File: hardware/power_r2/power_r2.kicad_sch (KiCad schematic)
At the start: 52 parts, among them J101 FPC Connector, J102 Power Input, Q101 AONR21357, U101 SIC473

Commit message: Next revision of the boards are finished and ready for fabrication, and a BOM has been added.
The BOM is still missing components for the nucleo shield.
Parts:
- added TP106: GND Test Point, TestPoint:TestPoint_Pad_D1.5mm, symbol Connector:TestPoint
- C104, C105: Item Link https://www.digikey.com.au/en/products/detail/murata-electr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 -> https://www.digikey.com.au/en/products/detail/stmicroelectr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
- C106: value 100n -> 100n 100V; Item Link Use existing -> https://www.digikey.com.au/en/products/detail/stmicroelectr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
- C107, C108, C109, C110, C111, C112: Item Link Use existing -> https://www.digikey.com.au/en/products/detail/samsung-elect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
- C113, C115: Item Link (none) -> https://www.digikey.com.au/en/products/detail/murata-electr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
- C114: Item Link Use existing -> https://www.digikey.com.au/en/products/detail/murata-electr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
- C116: Item Link https://www.digikey.com.au/en/products/detail/tdk-corporati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 -> https://www.digikey.com.au/en/products/detail/murata-electr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
- C117: Item Link https://www.digikey.com.au/en/products/detail/w%C3%BCrth-el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 -> https://www.digikey.com.au/en/products/detail/yageo/CC0603J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
- C118: value 100n 50V -> 100n 100V; Item Link (none) -> https://www.digikey.com.au/en/products/detail/stmicroelectr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
- C119: value 100n -> 100n 100V; Item Link (none) -> https://www.digikey.com.au/en/products/detail/stmicroelectr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
- H101, H102, JP104, TP101, TP102, TP103, TP104, TP105: now left out of the parts list
- J101: Item Link (none) -> https://www.digikey.com.au/en/products/detail/cvilux-usa/CF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
- J102: Item Link (none) -> https://au.element14.com/jst-japan-solderless-terminals/s2b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
- JP101, JP102, JP103: footprint Jumper:SolderJumper-3_P1.3mm_Open_Pad1.0x1.5mm -> rave_shades:SolderJumper-3_P1.3mm_Open_Pad1.0x1.5mm; now left out of the parts list
- R101, R109, R114: value 10k -> 10k 1%; Item Link (none) -> https://www.digikey.com.au/en/products/detail/bourns-inc/CR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
- R102, R103, R104, R105, R106, R108, R111, R112: Item Link (none) -> https://www.digikey.com.au/en/products/detail/yageo/RC0402F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
- R107: Item Link (none) -> https://www.digikey.com.au/en/products/detail/bourns-inc/CR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
- R110: Item Link (none) -> https://www.digikey.com.au/en/products/detail/stackpole-ele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
- R113: Item Link (none) -> https://www.digikey.com.au/en/products/detail/koa-speer-ele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
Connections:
- net +5V: now also J101.7 (Pin_7); no longer J101.2 (Pin_2)
- net GND: now also TP106.1
- net SPARE_0_5V0: now also J101.2 (Pin_2); no longer J101.7 (Pin_7)
- net SPARE_1_5V0: now also J101.1 (Pin_1); no longer J101.8 (Pin_8)
- net +5V_OR_GND renamed 5V0_OR_GND
- net 5V0_OR_GND: now also J101.8 (Pin_8); no longer J101.1 (Pin_1)
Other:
- note added: "Over Current Protection Imax = 3 A R = 0.024 R Vmax = 32 V"
- note removed: "ESD Protection Imax = 3 A R = 0.024 R Vmax = 32 V"
- moved on the sheet: C101, C102, C103, C104, C105, C106, C107, C108, C109, C110, C111, C112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

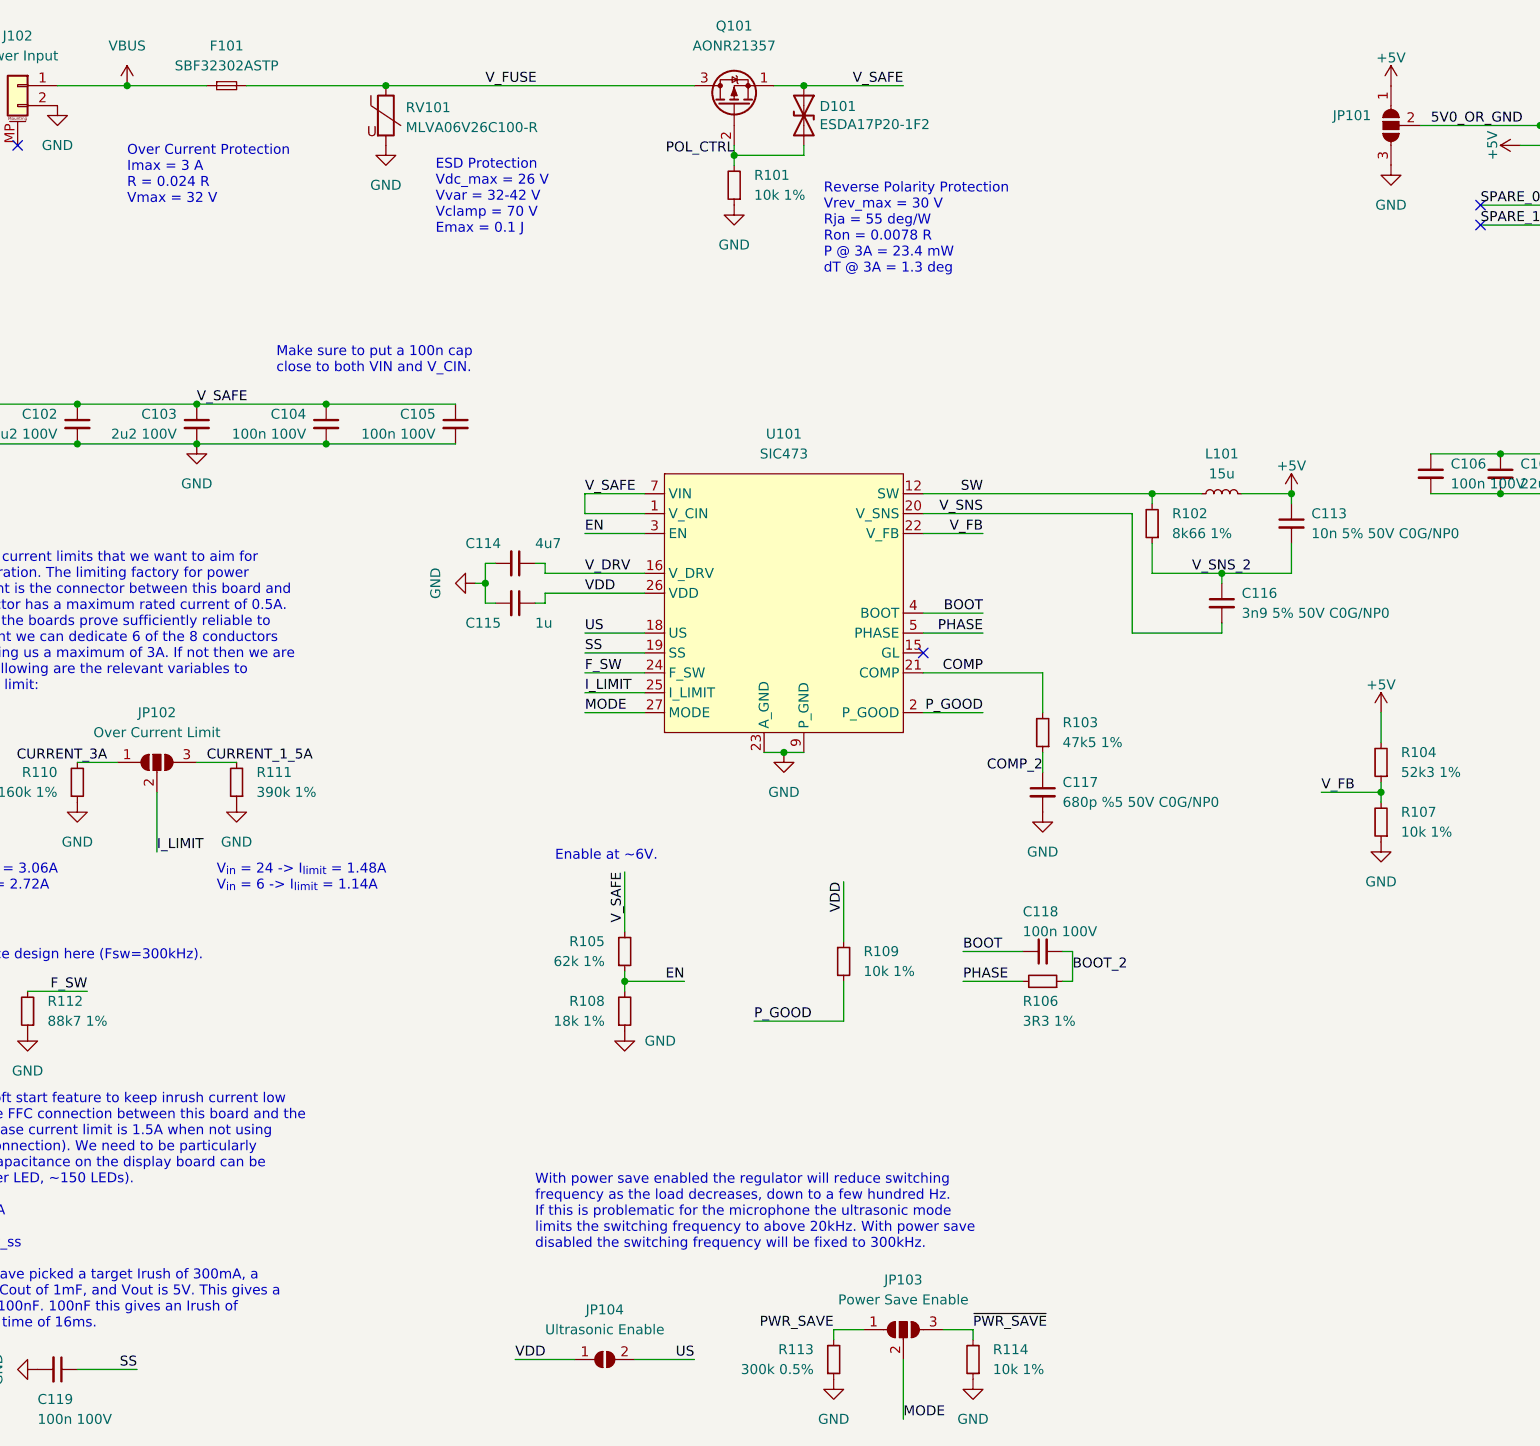
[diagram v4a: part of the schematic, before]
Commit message: Updated kicad files to work with latest kicad. Added some todos for next hw design.
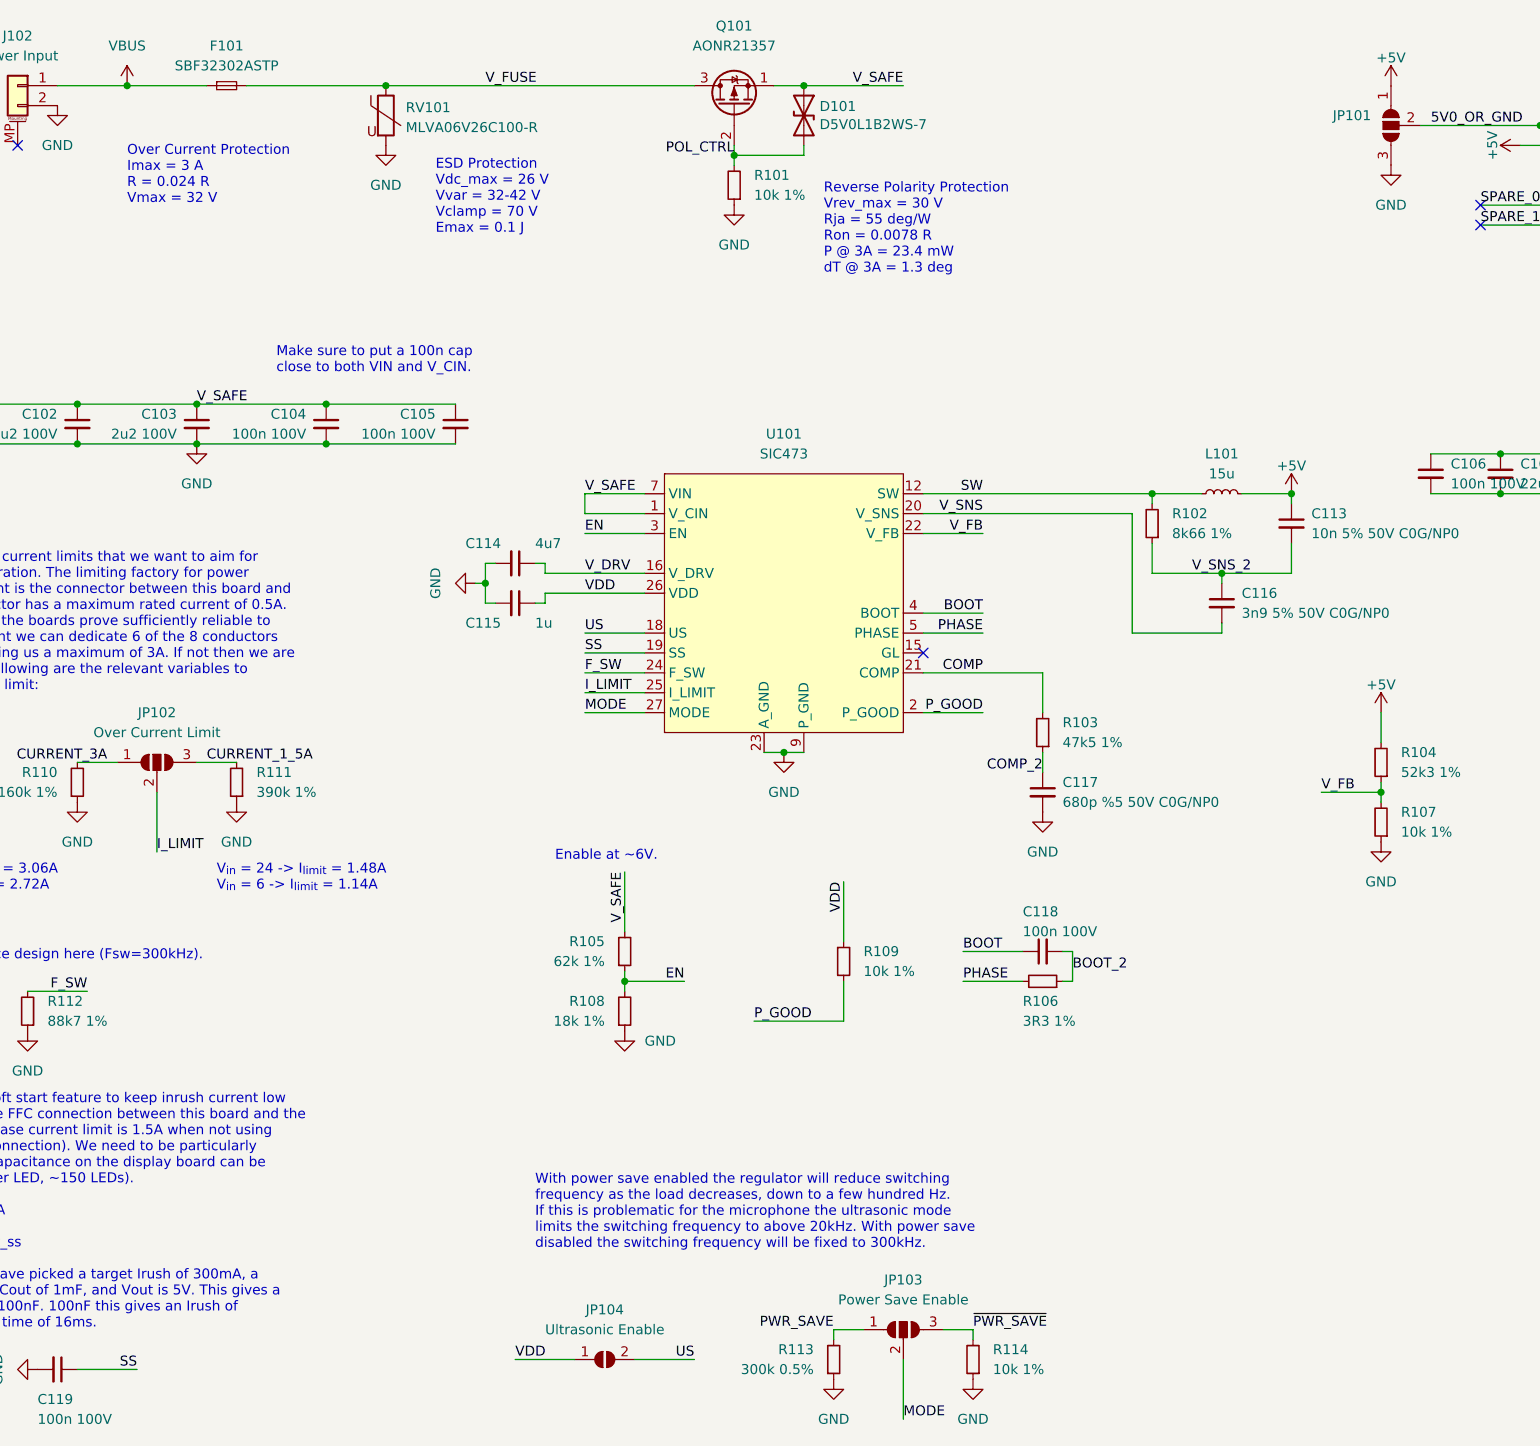
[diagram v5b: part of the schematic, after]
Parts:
- C104, C105, C106, C118, C119: Item Link https://www.digikey.com.au/en/products/detail/stmicroelectr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 -> https://www.digikey.com.au/en/products/detail/murata-electr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
- D101: value ESDA17P20-1F2 -> D5V0L1B2WS-7; Item Link https://www.digikey.com.au/en/products/detail/stmicroelectr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 -> https://www.digikey.com.au/en/products/detail/diodes-incorp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
